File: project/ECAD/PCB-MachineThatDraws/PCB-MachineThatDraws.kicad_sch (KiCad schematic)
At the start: 15 parts, among them J1 SD_Card_Device, J2 SDA/SCL/VCC/GND, J3 Switch, J4 Switch, J5 Moteur, J6 Moteur, U1 ESP32-S3-UNO

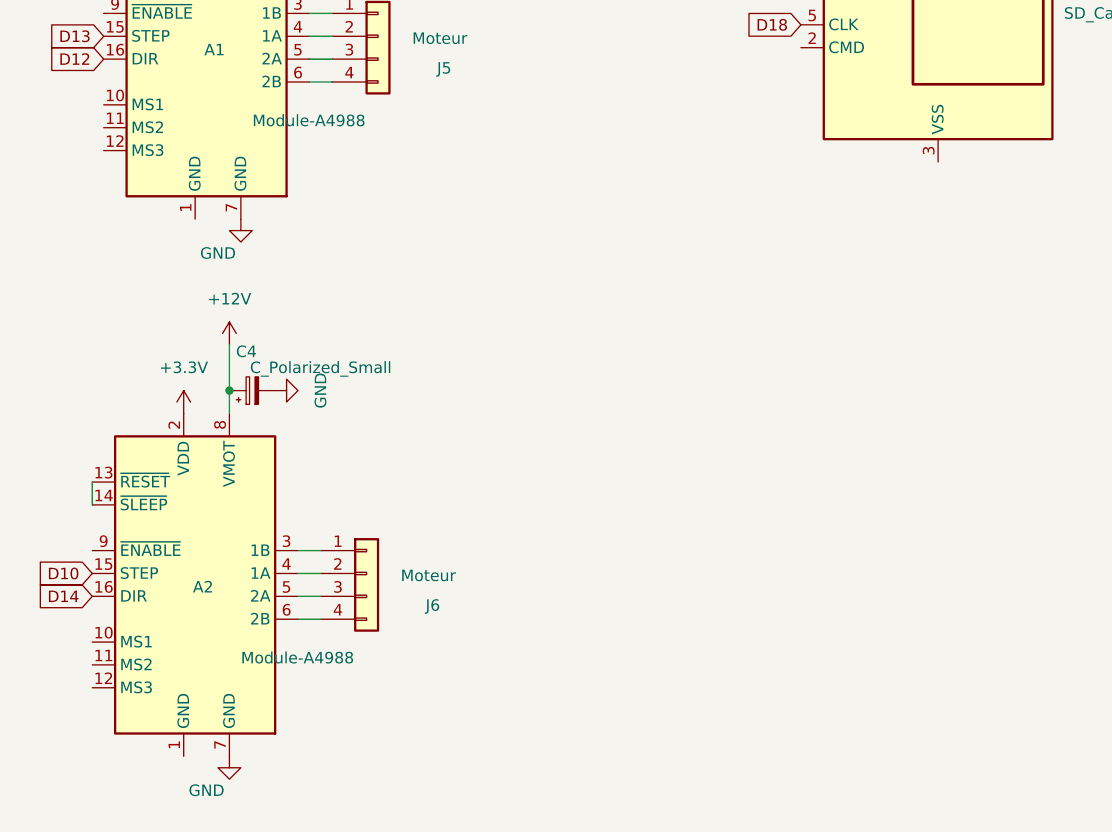
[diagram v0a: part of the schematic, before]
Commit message: cervo+regul5V
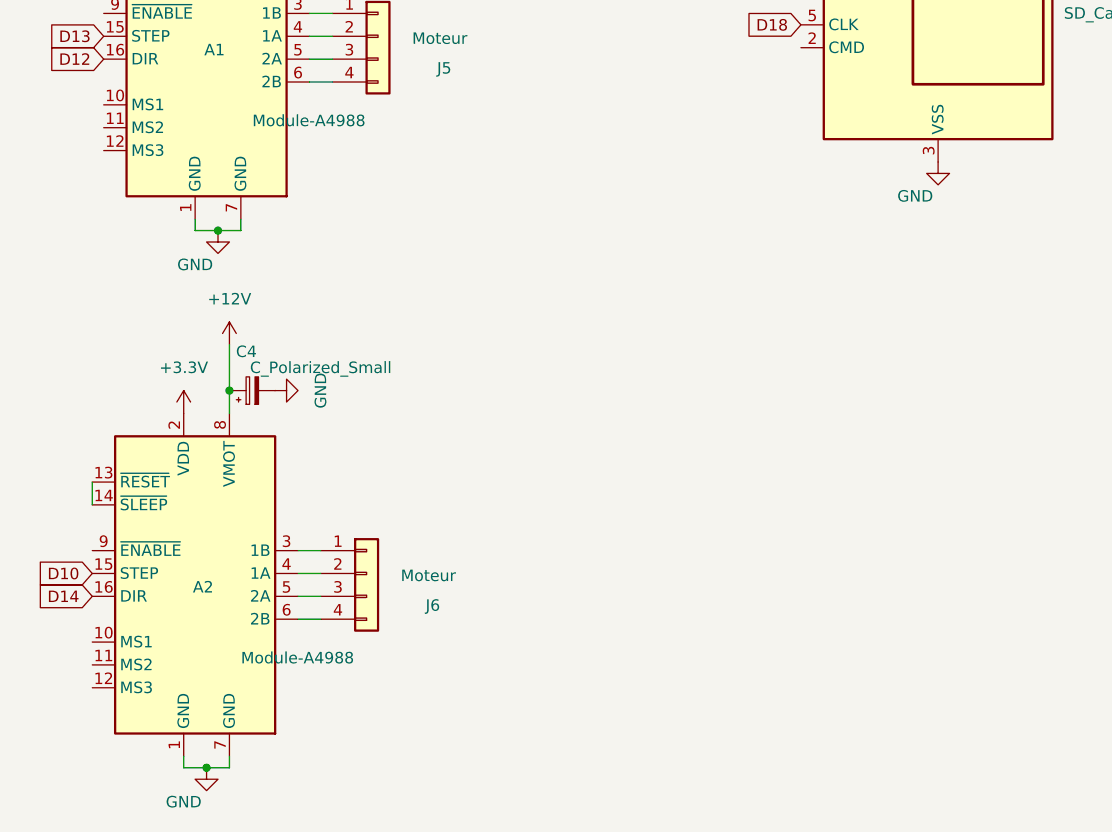
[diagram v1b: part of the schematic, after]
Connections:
- net GND: now also A1.1 (GND), A2.1 (GND), J1.3 (VSS), J1.6 (VSS)
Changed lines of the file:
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@@
+	)
+	(junction
+		(at 154.94 83.82)
+		(diameter 0)
+		(color 0 0 0 0)
 	)
 	(junction
@@
 	)
 	(junction
+		(at 153.67 143.51)
+		(diameter 0)
+		(color 0 0 0 0)
+	)
+	(junction
 		(at 38.1 110.49)
 		(diameter 0)
@@
 	(wire
 		(pts
+			(xy 157.48 83.82) (xy 157.48 82.55)
+		)
+		(stroke
+			(width 0)
+			(type default)
+		)
+	)
+	(wire
+		(pts
 			(xy 29.21 116.84) (xy 38.1 116.84)
 		)
@@
 	(wire
 		(pts
+			(xy 156.21 143.51) (xy 153.67 143.51)
+		)
+		(stroke
+			(width 0)
+			(type default)
+		)
+	)
+	(wire
+		(pts
 			(xy 38.1 110.49) (xy 38.1 109.22)
 		)
@@
 	(wire
 		(pts
+			(xy 154.94 83.82) (xy 157.48 83.82)
+		)
+		(stroke
+			(width 0)
+			(type default)
+		)
+	)
+	(wire
+		(pts
 			(xy 38.1 110.49) (xy 53.34 110.49)
 		)
@@
 	(wire
 		(pts
+			(xy 156.21 143.51) (xy 156.21 142.24)
+		)
+		(stroke
+			(width 0)
+			(type default)
+		)
+	)
+	(wire
+		(pts
 			(xy 166.37 121.92) (xy 163.83 121.92)
 		)
@@
 	(wire
 		(pts
+			(xy 151.13 142.24) (xy 151.13 143.51)
+		)
+		(stroke
+			(width 0)
+			(type default)
+		)
+	)
+	(wire
+		(pts
 			(xy 166.37 124.46) (xy 163.83 124.46)
 		)
@@
 	(wire
 		(pts
+			(xy 152.4 83.82) (xy 154.94 83.82)
+		)
+		(stroke
+			(width 0)
+			(type default)
+		)
+	)
+	(wire
+		(pts
 			(xy 167.64 67.31) (xy 165.1 67.31)
 		)
@@
 	(wire
 		(pts
+			(xy 152.4 82.55) (xy 152.4 83.82)
+		)
+		(stroke
+			(width 0)
+			(type default)
+		)
+	)
+	(wire
+		(pts
 			(xy 167.64 59.69) (xy 165.1 59.69)
+		)
+		(stroke
+			(width 0)
+			(type default)
+		)
+	)
+	(wire
+		(pts
+			(xy 151.13 143.51) (xy 153.67 143.51)
 		)
 		(stroke
@@
 	(symbol
 		(lib_id "power:GND")
-		(at 156.21 142.24 0)
+		(at 153.67 143.51 0)
 		(unit 1)
 		(exclude_from_sim no)
@@
 		(dnp no)
 		(property "Reference" "#PWR019"
-			(at 156.21 148.59 0)
+			(at 153.67 149.86 0)
 			(effects
 				(font
@@
 		)
 		(property "Value" "GND"
-			(at 153.67 146.05 0)
+			(at 151.13 147.32 0)
 			(effects
 				(font
@@
 		)
 		(property "Footprint" ""
-			(at 156.21 142.24 0)
+			(at 153.67 143.51 0)
 			(effects
 				(font
@@
 		)
 		(property "Datasheet" ""
-			(at 156.21 142.24 0)
+			(at 153.67 143.51 0)
 			(effects
 				(font
@@
 		)
 		(property "Description" "Power symbol creates a global label with name \"GND\" , ground"
-			(at 156.21 142.24 0)
+			(at 153.67 143.51 0)
 			(effects
 				(font
@@
 	)
 	(symbol
+		(lib_id "power:GND")
+		(at 234.95 76.2 0)
+		(unit 1)
+		(exclude_from_sim no)
+		(in_bom yes)
+		(on_board yes)
+		(dnp no)
+		(property "Reference" "#PWR024"
+			(at 234.95 82.55 0)
+			(effects
+				(font
+					(size 1.27 1.27)
+				)
+				(hide yes)
+			)
+		)
+		(property "Value" "GND"
+			(at 232.41 80.01 0)
+			(effects
+				(font
+					(size 1.27 1.27)
+				)
+			)
+		)
+		(property "Footprint" ""
+			(at 234.95 76.2 0)
+			(effects
+				(font
+					(size 1.27 1.27)
+				)
+				(hide yes)
+			)
+		)
+		(property "Datasheet" ""
+			(at 234.95 76.2 0)
+			(effects
+				(font
+					(size 1.27 1.27)
+				)
+				(hide yes)
+			)
+		)
+		(property "Description" "Power symbol creates a global label with name \"GND\" , ground"
+			(at 234.95 76.2 0)
+			(effects
+				(font
+					(size 1.27 1.27)
+				)
+				(hide yes)
+			)
+		)
+		(pin "1"
+		)
+		(instances
+			(project "PCB-MachineThatDraws"
+				(path "/d1309c4d-f5c5-4ae1-9a0a-1ebc6300afdd"
+					(reference "#PWR024")
+					(unit 1)
+				)
+			)
+		)
+	)
+	(symbol
 		(lib_id "power:+5V")
 		(at 157.48 36.83 0)
@@
 	(symbol
 		(lib_id "power:GND")
-		(at 157.48 82.55 0)
+		(at 154.94 83.82 0)
 		(unit 1)
 		(exclude_from_sim no)
@@
 		(dnp no)
 		(property "Reference" "#PWR09"
-			(at 157.48 88.9 0)
+			(at 154.94 90.17 0)
 			(effects
 				(font
@@
 		)
 		(property "Value" "GND"
-			(at 154.94 86.36 0)
+			(at 152.4 87.63 0)
 			(effects
 				(font
@@
 		)
 		(property "Footprint" ""
-			(at 157.48 82.55 0)
+			(at 154.94 83.82 0)
 			(effects
 				(font
@@
 		)
 		(property "Datasheet" ""
-			(at 157.48 82.55 0)
+			(at 154.94 83.82 0)
 			(effects
 				(font
@@
 		)
 		(property "Description" "Power symbol creates a global label with name \"GND\" , ground"
-			(at 157.48 82.55 0)
-			(effects
-				(font
+			(at 154.94 83.82 0)
+			(effects
+				(font

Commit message: Update PCB-MachineThatDraws.kicad_sch
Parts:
- removed C2: C, makerspace-unilasalle:C_1206, symbol Device:C
- added C5, C6: 10µF, symbol Device:C
- added C7: C_Polarized_Small, symbol Device:C_Polarized_Small
- added C8: C_Small, symbol Device:C_Small
- added F1: Fuse, symbol makerspace-unilasalle:Fuse
- added J10, J11: Conn_02x03_Odd_Even, Connector_PinHeader_2.54mm:PinHeader_2x03_P2.54mm_Vertical, symbol Connector_Generic:Conn_02x03_Odd_Even
- added J7: Barrel_Jack_Switch, symbol makerspace-unilasalle:Barrel_Jack_Switch
- added J8: Screw_Terminal_01x02, symbol makerspace-unilasalle:Screw_Terminal_01x02
- added J9: Servo, symbol makerspace-unilasalle:Conn_01x03
- added R3: 1K, symbol Device:R
- added U2: R-78E5.0-1.0, Converter_DCDC:Converter_DCDC_RECOM_R-78E-0.5_THT, symbol makerspace-unilasalle:R-78E5.0-1.0
- C1: value C_Polarized_Small -> ?uF
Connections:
- net +12V: now also C5.1, F1.2, U2.1 (IN)
- net +3.3V: now also J2.3 (Pin_3), C8.1, J10.1 (Pin_1), J10.3 (Pin_3), J10.5 (Pin_5), J11.1 (Pin_1), J11.3 (Pin_3), J11.5 (Pin_5)
- net +5V: now also C6.1, C7.1, J9.2 (Pin_2), R3.1, U2.3 (OUT); no longer J2.3 (Pin_3)
- net GND: now also C5.2, C6.2, C7.2, C8.2, J7.2, J7.3, J9.3 (Pin_3), U2.2 (GND)
- net SCL: no longer R2.1
- net SCL : now also R2.1
- net SDA: now also R1.1
- net SDA : no longer R1.1
- net at A1.10 (MS1): now also J11.2 (Pin_2)
- net at A1.11 (MS2): now also J11.4 (Pin_4)
- net at A1.12 (MS3): now also J11.6 (Pin_6)
- net Enable: now reaches A1.9 (~{ENABLE})
- net Enable: now also A2.9 (~{ENABLE})
- net D07: now reaches U1.11 (GPIO7/ADC1_CH6)
- net D07: now also J9.1 (Pin_1)
- net at A2.10 (MS1): now also J10.2 (Pin_2)
- net at A2.11 (MS2): now also J10.4 (Pin_4)
- net at A2.12 (MS3): now also J10.6 (Pin_6)
- new net: J7.1, J8.1 (Pin_1)
- new net: F1.1, J8.2 (Pin_2)
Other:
- moved on the sheet: A1, A2, C1, C3, C4, J2, J3, J4, J5, J6, R1, R2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

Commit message: Update PCB-MachineThatDraws.kicad_sch
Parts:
- added D1: LED, symbol Device:LED
- J1: footprint (none) -> Connector_Card:SD_Card_Device_16mm_SlotDepth
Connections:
- net +5V: now also U1.8 (VIN)
- net at R3.2: now also D1.2 (A)
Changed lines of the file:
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@@
 	(wire
 		(pts
+			(xy 88.9 48.26) (xy 88.9 50.8)
+		)
+		(stroke
+			(width 0)
+			(type default)
+		)
+	)
+	(wire
+		(pts
 			(xy 113.03 147.32) (xy 113.03 146.05)
 		)
@@
 	)
 	(symbol
+		(lib_id "Device:LED")
+		(at 203.2 41.91 270)
+		(unit 1)
+		(exclude_from_sim no)
+		(in_bom yes)
+		(on_board yes)
+		(dnp no)
+		(fields_autoplaced yes)
+		(property "Reference" "D1"
+			(at 205.74 39.0524 90)
+			(effects
+				(font
+					(size 1.27 1.27)
+				)
+				(justify left)
+			)
+		)
+		(property "Value" "LED"
+			(at 205.74 41.5924 90)
+			(effects
+				(font
+					(size 1.27 1.27)
+				)
+				(justify left)
+			)
+		)
+		(property "Footprint" ""
+			(at 203.2 41.91 0)
+			(effects
+				(font
+					(size 1.27 1.27)
+				)
+				(hide yes)
+			)
+		)
+		(property "Datasheet" "~"
+			(at 203.2 41.91 0)
+			(effects
+				(font
+					(size 1.27 1.27)
+				)
+				(hide yes)
+			)
+		)
+		(property "Description" "Light emitting diode"
+			(at 203.2 41.91 0)
+			(effects
+				(font
+					(size 1.27 1.27)
+				)
+				(hide yes)
+			)
+		)
+		(property "Sim.Pins" "1=K 2=A"
+			(at 203.2 41.91 0)
+			(effects
+				(font
+					(size 1.27 1.27)
+				)
+				(hide yes)
+			)
+		)
+		(pin "2"
+		)
+		(pin "1"
+		)
+		(instances
+			(project ""
+				(path "/d1309c4d-f5c5-4ae1-9a0a-1ebc6300afdd"
+					(reference "D1")
+					(unit 1)
+				)
+			)
+		)
+	)
+	(symbol
 		(lib_id "Device:C_Polarized_Small")
 		(at 114.3 142.24 0)
@@
 	(symbol
 		(lib_id "power:+5V")
+		(at 85.09 50.8 0)
+		(unit 1)
+		(exclude_from_sim no)
+		(in_bom yes)
+		(on_board yes)
+		(dnp no)
+		(fields_autoplaced yes)
+		(property "Reference" "#PWR03"
+			(at 85.09 54.61 0)
+			(effects
+				(font
+					(size 1.27 1.27)
+				)
+				(hide yes)
+			)
+		)
+		(property "Value" "+5V"
+			(at 85.09 45.72 0)
+			(effects
+				(font
+					(size 1.27 1.27)
+				)
+			)
+		)
+		(property "Footprint" ""
+			(at 85.09 50.8 0)
+			(effects
+				(font
+					(size 1.27 1.27)
+				)
+				(hide yes)
+			)
+		)
+		(property "Datasheet" ""
+			(at 85.09 50.8 0)
+			(effects
+				(font
+					(size 1.27 1.27)
+				)
+				(hide yes)
+			)
+		)
+		(property "Description" "Power symbol creates a global label with name \"+5V\""
+			(at 85.09 50.8 0)
+			(effects
+				(font
+					(size 1.27 1.27)
+				)
+				(hide yes)
+			)
+		)
+		(pin "1"
+		)
+		(instances
+			(project "PCB-MachineThatDraws"
+				(path "/d1309c4d-f5c5-4ae1-9a0a-1ebc6300afdd"
+					(reference "#PWR03")
+					(unit 1)
+				)
+			)
+		)
+	)
+	(symbol
+		(lib_id "power:+5V")
 		(at 168.91 41.91 0)
 		(unit 1)
@@
 			)
 		)
-		(property "Footprint" ""
+		(property "Footprint" "Connector_Card:SD_Card_Device_16mm_SlotDepth"
 			(at 234.95 58.42 0)
 			(effects
@@
 	(symbol
 		(lib_id "power:+3.3V")
-		(at 88.9 50.8 0)
+		(at 88.9 48.26 0)
 		(unit 1)
 		(exclude_from_sim no)
@@
 		(fields_autoplaced yes)
 		(property "Reference" "#PWR021"
-			(at 88.9 54.61 0)
+			(at 88.9 52.07 0)
 			(effects
 				(font
@@
 		)
 		(property "Value" "+3.3V"
-			(at 88.9 45.72 0)
+			(at 88.9 43.18 0)
 			(effects
 				(font
@@
 		)
 		(property "Footprint" ""
-			(at 88.9 50.8 0)
+			(at 88.9 48.26 0)
 			(effects
 				(font
@@
 		)
 		(property "Datasheet" ""
-			(at 88.9 50.8 0)
+			(at 88.9 48.26 0)
 			(effects
 				(font
@@
 		)
 		(property "Description" "Power symbol creates a global label with name \"+3.3V\""
-			(at 88.9 50.8 0)
+			(at 88.9 48.26 0)
 			(effects
 				(font
@@
 		(pin "18"
 		)
+		(pin "8"
+		)
 		(instances

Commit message: pcb add
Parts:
- removed D1: LED, symbol Device:LED
- added D1: Green, LED_SMD:LED_1206_3216Metric, symbol Device:LED_Small
- added R4, R5: 10k, makerspace-unilasalle:R_1206, symbol makerspace-unilasalle:R
- C1: value ?uF -> 100µF; footprint (none) -> makerspace-unilasalle:C_1206
- C3, C4: footprint (none) -> Capacitor_SMD:CP_Elec_6.3x5.4
- C5, C6: footprint (none) -> makerspace-unilasalle:C_1206
- C7: value C_Polarized_Small -> 10uF; footprint (none) -> makerspace-unilasalle:C_1206
- C8: value C_Small -> 100nF; footprint (none) -> makerspace-unilasalle:C_1206
- F1: footprint (none) -> Fuse:Fuseholder_Blade_Mini_Keystone_3568
- J4: value Switch -> Limit_Switch_X
- J7: footprint (none) -> Connector_BarrelJack:BarrelJack_GCT_DCJ200-10-A_Horizontal
- J8: footprint (none) -> TerminalBlock:TerminalBlock_bornier-2_P5.08mm
- J9: footprint (none) -> Connector:FanPinHeader_1x03_P2.54mm_Vertical
- R1, R2, R3: footprint (none) -> makerspace-unilasalle:R_1206
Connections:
- net +3.3V: now also R4.2, R5.2
- net D05: now also R4.1
- net D11: now also J1.2 (CMD); no longer J1.9 (DAT2)
- net D19: now also J1.7 (DAT0), R5.1; no longer J1.8 (DAT1)
- net Enable: now also U1.24 (GPIO46)
- net GND: now also D1.1 (K)
- net at R3.2: now also D1.2 (A)
- no-connect marks 0 -> 11
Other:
- moved on the sheet: J1

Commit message: new
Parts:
- J2, J5, J6: footprint Connector_JST:JST_PH_B3B-PH-K_1x04_P2.00mm_Vertical -> Connector:NS-Tech_Grove_1x04_P2mm_Vertical
- U1: footprint PCM_Espressif:ESP32-S3-DevKitC -> makerspace-unilasalle:ESP_S3_UNO
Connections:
- net D19: now also U1.12 (GPIO6/ADC1_CH5); no longer U1.19 (GPIO19/USB_D-)
- no-connect marks 11 -> 16
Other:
- moved on the sheet: J3, J4, U1

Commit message: 10-04
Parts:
- J1: footprint Connector_Card:SD_Card_Device_16mm_SlotDepth -> makerspace-unilasalle:SD_Hirose_DM1AA_SF_PEJ82
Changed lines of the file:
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@@
 	(wire
 		(pts
-			(xy 168.91 41.91) (xy 168.91 45.72)
+			(xy 168.91 40.64) (xy 168.91 45.72)
 		)
 		(stroke
@@
 	(symbol
 		(lib_id "power:+5V")
-		(at 168.91 41.91 0)
+		(at 168.91 40.64 0)
 		(unit 1)
 		(exclude_from_sim no)
@@
 		(fields_autoplaced yes)
 		(property "Reference" "#PWR026"
-			(at 168.91 45.72 0)
+			(at 168.91 44.45 0)
 			(effects
 				(font
@@
 		)
 		(property "Value" "+12V"
-			(at 168.91 36.83 0)
+			(at 168.91 35.56 0)
 			(effects
 				(font
@@
 		)
 		(property "Footprint" ""
-			(at 168.91 41.91 0)
+			(at 168.91 40.64 0)
 			(effects
 				(font
@@
 		)
 		(property "Datasheet" ""
-			(at 168.91 41.91 0)
+			(at 168.91 40.64 0)
 			(effects
 				(font
@@
 		)
 		(property "Description" "Power symbol creates a global label with name \"+5V\""
-			(at 168.91 41.91 0)
+			(at 168.91 40.64 0)
 			(effects
 				(font
@@
 			)
 		)
-		(property "Footprint" "Connector_Card:SD_Card_Device_16mm_SlotDepth"
+		(property "Footprint" "makerspace-unilasalle:SD_Hirose_DM1AA_SF_PEJ82"
 			(at 255.27 59.69 0)
 			(effects
